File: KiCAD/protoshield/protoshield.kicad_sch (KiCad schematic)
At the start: 35 parts, among them J1 Screw_Terminal_01x03, J2 Screw_Terminal_01x02, J3 Screw_Terminal_01x02, J4 Screw_Terminal_01x02, J5 Screw_Terminal_01x02, J6 Screw_Terminal_01x03, J7 Screw_Terminal_01x04, J8 Screw_Terminal_01x03, U2 Metro_ESP32S3

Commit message: revD: DGFET-DAC bias scheme, kit-style xfmr naming, custom footprints, Output LPF project
Architecture refinements since the previous revD commit (f8d7058):

Analog board (vfo_complete, arduino, dac, power sheets):
  * MCP4922 (U4) ch B exposed as DRIVER_BIAS DAC output -> J31 pin 6
    (replaces the +3.3V pin that was on J31 pin 6 before). Analog's U4
    now controls the ss_pa BS170 driver DC bias point directly from
    firmware -- cleaner than the kit's trimmer+Q201 scheme.
  * MCP4728 (U3) ch A/B exposed as PA_Bias_A_Raw / PA_Bias_B_Raw ->
    J31 pins 7, 8. These feed the ss_pa CD74HC4066 fault-switch (U2),
    which gates them to PA_Bias_A/B on the IRF510 gates. On FAULT_N
    low, switch opens -> IRF510 bias collapses -> conduction cuts.
  * Rename pass: Bias_A/B/_Raw labels -> PA_Bias_A/B/_Raw everywhere
    (analog J3 screw-terminal, umbilical J31, ss_pa U2 inputs). Prefix
    disambiguates from DRIVER_BIAS which drives a different stage.
  * J2 (band-select RJ45 to Output LPF board): added RLY_40 provision.
    Pin layout reorganized -- RLY_40 lives at pin 5, pin 6 kept as a
    spare for a future 6th band.

ss_pa board (pa_stage, fault_shutdown, lpf sheets):
  * Driver + final BS170/IRF510 topology drawn following QRP Labs
    10W Linear kit (RF IN -> T201 input xfmr -> BS170 PP driver
    (Q2, Q6) -> T202 interstage -> IRF510 PP finals (Q3, Q4) ->
    T203 bifilar drain feed -> T204 output xfmr -> RF out).
  * Transformer references renamed to match the kit: T201 (input,
    BN61-2402), T202 (interstage, BN61-2402), T203 (drain feed,
    T50-43), T204 (output, BN43-202).
  * Driver bias filter on DRIVER_BIAS: C19 (0.1uF) + C20 (100pF)
    bulk + HF bypass, into T201 secondary CT (pin 4).
  * +3.3V now locally regulated on ss_pa (MCP1700x-330xxTO, U13)
    from +13.8V, powering U1 (LM393) and U2 (CD74HC4066). J31
    pin 6 freed up for DRIVER_BIAS.
  * Duplicate RJ45 J7 deleted (was a leftover from pre-DAC-bias era).
  * J3 (SMA RF input from analog) foo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
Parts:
- C2, C3: footprint (none) -> Capacitor_THT:C_Disc_D6.0mm_W2.5mm_P5.00mm
- J7: footprint (none) -> TerminalBlock_Phoenix:TerminalBlock_Phoenix_MKDS-1,5-4_1x04_P5.00mm_Horizontal
- J8: footprint (none) -> TerminalBlock_Phoenix:TerminalBlock_Phoenix_MKDS-1,5-3_1x03_P5.00mm_Horizontal
- R1, R2: footprint (none) -> Resistor_THT:R_Axial_DIN0207_L6.3mm_D2.5mm_P10.16mm_Horizontal
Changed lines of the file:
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@@
 			)
 		)
-		(property "Footprint" ""
+		(property "Footprint" "TerminalBlock_Phoenix:TerminalBlock_Phoenix_MKDS-1,5-4_1x04_P5.00mm_Horizontal"
 			(at 232.41 104.14 0)
 			(hide yes)
@@
 			)
 		)
-		(property "Footprint" ""
+		(property "Footprint" "Resistor_THT:R_Axial_DIN0207_L6.3mm_D2.5mm_P10.16mm_Horizontal"
 			(at 198.374 87.884 90)
 			(hide yes)
@@
 			)
 		)
-		(property "Footprint" ""
+		(property "Footprint" "Resistor_THT:R_Axial_DIN0207_L6.3mm_D2.5mm_P10.16mm_Horizontal"
 			(at 198.374 85.344 90)
 			(hide yes)
@@
 			)
 		)
-		(property "Footprint" ""
+		(property "Footprint" "Capacitor_THT:C_Disc_D6.0mm_W2.5mm_P5.00mm"
 			(at 195.2752 96.52 0)
 			(hide yes)
@@
 			)
 		)
-		(property "Footprint" ""
+		(property "Footprint" "Capacitor_THT:C_Disc_D6.0mm_W2.5mm_P5.00mm"
 			(at 193.3448 78.74 0)
 			(hide yes)
@@
 			)
 		)
-		(property "Footprint" ""
+		(property "Footprint" "TerminalBlock_Phoenix:TerminalBlock_Phoenix_MKDS-1,5-3_1x03_P5.00mm_Horizontal"
 			(at 213.36 88.9 0)
 			(hide yes)

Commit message: revD: ss_pa Option C 5V rail + analog SW1 THT + R/C footprints + doc refresh
ss_pa Option C: swap U13 to LM2936Z-5.0 (full +5V logic rail), re-size
R10 10K->6.8K to preserve ~0.3V fault trip at new rail, drop +3.3V net
entirely. Fixes the previously-dead +5V bus that had no source.

Analog SW1 (Si5351 bringup DPDT): swap SMD footprint for
Button_Switch_THT:SW_CK_JS202011CQN_DPDT_Straight. Verified pin-numbering
convention (pin 1 above pin 6 in THT) matches user's intended DPST
wiring; both SDA/SCL break together.

Analog: assign missing footprints to R3/R4/R5/R8/R9 (DIN0207 axial) and
C4/C5/C6/C7/C8 (disc ceramic 5mm). Add xmitter:DIP-14_W7.62mm.kicad_mod
and 74HCT125 symbol to the xmitter library.

Documentation: Rev D handoff doc updated with M1-M8 fix status, Option C
notes, I2C bus voltage architecture, 74HCT125 SPI shifter, FAULT_N
divider details, and Metro-no-footprint note. Supporting docs updated:
i2c_bus.md full rewrite for 5V HV bus + STEMMA reroute, revD_interconnect
board inventory refresh, status banners on ss_pa.md / Master_Description /
cw_envelope_keyer / front_panel_interface pointing to handoff doc for
items beyond their last-current date.

Co-Authored-By: Claude Opus 4.7 <noreply@anthropic.com>
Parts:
- removed J7: Screw_Terminal_01x04, TerminalBlock_Phoenix:TerminalBlock_Phoenix_MKDS-1,5-4_1x04_P5.00mm_Horizontal, symbol Connector:Screw_Terminal_01x04
- added J17: Screw_Terminal_01x05, TerminalBlock_Phoenix:TerminalBlock_Phoenix_MKDS-1,5-5_1x05_P5.00mm_Horizontal, symbol Connector:Screw_Terminal_01x05
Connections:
- net CS_DAC: now also J17.5 (Pin_5)
- net DAC_LDAC_N: now also J17.2 (Pin_2)
- net GND: now also J17.1 (Pin_1)
- net MOSI: now also J17.4 (Pin_4)
- net SCK: now also J17.3 (Pin_3)
- net FAULT_N renamed FAULT_N_CLEAN
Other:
- moved on the sheet: J8
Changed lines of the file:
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@@
 	(wire
 		(pts
-			(xy 208.28 86.36) (xy 201.93 86.36)
+			(xy 217.17 86.36) (xy 201.93 86.36)
 		)
 		(stroke
@@
 	(wire
 		(pts
-			(xy 208.28 88.9) (xy 201.93 88.9)
+			(xy 217.17 88.9) (xy 201.93 88.9)
 		)
 		(stroke
@@
 		)
 	)
-	(global_label "FAULT_N"
+	(global_label "FAULT_N_CLEAN"
 		(shape input)
 		(at 161.29 91.44 0)
@@
 		)
 		(property "Intersheetrefs" "${INTERSHEET_REFS}"
-			(at 172.0767 91.44 0)
+			(at 178.9105 91.44 0)
 			(hide yes)
 			(show_name no)
@@
 	)
 	(global_label "DAC_LDAC_N"
-		(shape output)
-		(at 213.36 109.22 0)
+		(shape input)
+		(at 227.33 109.22 180)
 		(fields_autoplaced yes)
 		(effects
@@
 				(size 1.27 1.27)
 			)
-			(justify left)
+			(justify right)
 		)
 		(property "Intersheetrefs" "${INTERSHEET_REFS}"
-			(at 227.8962 109.22 0)
+			(at 212.7938 109.22 0)
 			(hide yes)
 			(show_name no)
@@
 					(size 1.27 1.27)
 				)
-				(justify left)
+				(justify right)
 			)
 		)
@@
 		)
 	)
-	(global_label "FAULT_N"
+	(global_label "FAULT_N_CLEAN"
 		(shape output)
-		(at 208.28 91.44 180)
+		(at 217.17 91.44 180)
 		(fields_autoplaced yes)
 		(effects
@@
 		)
 		(property "Intersheetrefs" "${INTERSHEET_REFS}"
-			(at 197.4933 91.44 0)
+			(at 199.5495 91.44 0)
 			(hide yes)
 			(show_name no)
@@
 	)
 	(symbol
-		(lib_id "Connector:Screw_Terminal_01x04")
-		(at 232.41 104.14 0)
-		(unit 1)
-		(body_style 1)
-		(exclude_from_sim no)
-		(in_bom yes)
-		(on_board yes)
-		(in_pos_files yes)
-		(dnp no)
-		(fields_autoplaced yes)
-		(property "Reference" "J7"
-			(at 234.95 104.1399 0)
-			(show_name no)
-			(do_not_autoplace no)
-			(effects
-				(font
-					(size 1.27 1.27)
-				)
-				(justify left)
-			)
-		)
-		(property "Value" "Screw_Terminal_01x04"
-			(at 234.95 106.6799 0)
-			(show_name no)
-			(do_not_autoplace no)
-			(effects
-				(font
-					(size 1.27 1.27)
-				)
-				(justify left)
-			)
-		)
-		(property "Footprint" "TerminalBlock_Phoenix:TerminalBlock_Phoenix_MKDS-1,5-4_1x04_P5.00mm_Horizontal"
-			(at 232.41 104.14 0)
-			(hide yes)
-			(show_name no)
-			(do_not_autoplace no)
-			(effects
-				(font
-					(size 1.27 1.27)
-				)
-			)
-		)
-		(property "Datasheet" ""
-			(at 232.41 104.14 0)
-			(hide yes)
-			(show_name no)
-			(do_not_autoplace no)
-			(effects
-				(font
-					(size 1.27 1.27)
-				)
-			)
-		)
-		(property "Description" "Generic screw terminal, single row, 01x04, script generated (kicad-library-utils/schlib/autogen/connector/)"
-			(at 232.41 104.14 0)
-			(hide yes)
-			(show_name no)
-			(do_not_autoplace no)
-			(effects
-				(font
-					(size 1.27 1.27)
-				)
-			)
-		)
-		(pin "3"
-		)
-		(pin "4"
-		)
-		(pin "2"
-		)
-		(pin "1"
-		)
-		(instances
-			(project "protoshield"
-				(path "/90f14230-179e-419d-8d57-3db6b8a7c39f"
-					(reference "J7")
-					(unit 1)
-				)
-			)
-		)
-	)
-	(symbol
 		(lib_id "power:GND")
 		(at 43.18 168.91 0)
@@
 		(in_pos_files yes)
 		(dnp no)
-		(fields_autoplaced yes)
 		(property "Reference" "#PWR014"
 			(at 227.33 78.74 0)
@@
 		)
 		(property "Value" "+3.3V"
-			(at 227.33 87.63 0)
+			(at 231.648 85.09 0)
 			(show_name no)
 			(do_not_autoplace no)
@@
 	(symbol
 		(lib_id "power:GND")
+		(at 227.33 111.76 0)
+		(unit 1)
+		(body_style 1)
+		(exclude_from_sim no)
+		(in_bom yes)
+		(on_board yes)
+		(in_pos_files yes)
+		(dnp no)
+		(fields_autoplaced yes)
+		(property "Reference" "#PWR024"
+			(at 227.33 118.11 0)
+			(hide yes)
+			(show_name no)
+			(do_not_autoplace no)
+			(effects
+				(font
+					(size 1.27 1.27)
+				)
+			)
+		)
+		(property "Value" "GND"
+			(at 227.33 116.84 0)
+			(show_name no)
+			(do_not_autoplace no)
+			(effects
+				(font
+					(size 1.27 1.27)
+				)
+			)
+		)
+		(property "Footprint" ""
+			(at 227.33 111.76 0)
+			(hide yes)
+			(show_name no)
+			(do_not_autoplace no)
+			(effects
+				(font
+					(size 1.27 1.27)
+				)
+			)
+		)
+		(property "Datasheet" ""
+			(at 227.33 111.76 0)
+			(hide yes)
+			(show_name no)
+			(do_not_autoplace no)
+			(effects
+				(font
+					(size 1.27 1.27)
+				)
+			)
+		)
+		(property "Description" "Power symbol creates a global label with name \"GND\" , ground"
+			(at 227.33 111.76 0)
+			(hide yes)
+			(show_name no)
+			(do_not_autoplace no)
+			(effects
+				(font
+					(size 1.27 1.27)
+				)
+			)
+		)
+		(pin "1"
+		)
+		(instances
+			(project "protoshield"
+				(path "/90f14230-179e-419d-8d57-3db6b8a7c39f"
+					(reference "#PWR024")
+					(unit 1)
+				)
+			)
+		)
+	)
+	(symbol
+		(lib_id "power:GND")
 		(at 128.27 69.85 270)
 		(unit 1)
@@
 	)
 	(symbol
+		(lib_id "Connector:Screw_Terminal_01x05")
+		(at 232.41 106.68 0)
+		(mirror x)
+		(unit 1)
+		(body_style 1)
+		(exclude_from_sim no)
+		(in_bom yes)
+		(on_board yes)
+		(in_pos_files yes)
+		(dnp no)
+		(property "Reference" "J17"
+			(at 232.41 95.25 0)
+			(show_name no)
+			(do_not_autoplace no)
+			(effects
+				(font
+					(size 1.27 1.27)
+				)
+			)
+		)
+		(property "Value" "Screw_Terminal_01x05"
+			(at 232.41 97.79 0)
+			(show_name no)
+			(do_not_autoplace no)
+			(effects
+				(font
+					(size 1.27 1.27)
+				)
+			)
+		)
+		(property "Footprint" "TerminalBlock_Phoenix:TerminalBlock_Phoenix_MKDS-1,5-5_1x05_P5.00mm_Horizontal"
+			(at 232.41 106.68 0)
+			(hide yes)
+			(show_name no)
+			(do_not_autoplace no)
+			(effects
+				(font
+					(size 1.27 1.27)
+				)
+			)
+		)
+		(property "Datasheet" ""
+			(at 232.41 106.68 0)
+			(hide yes)
+			(show_name no)
+			(do_not_autoplace no)
+			(effects
+				(font
+					(size 1.27 1.27)
+				)
+			)
+		)
+		(property "Description" "Generic screw terminal, single row, 01x05, script generated (kicad-library-utils/schlib/autogen/connector/)"
+			(at 232.41 106.68 0)
+			(hide yes)
+			(show_name no)
+			(do_not_autoplace no)
+			(effects
+				(font
+					(size 1.27 1.27)
+				)
+			)
+		)
+		(pin "1"
+		)
+		(pin "4"
+		)
+		(pin "5"
+		)
+		(pin "2"
+		)
+		(pin "3"
+		)
+		(instances
+			(project "protoshield"
+				(path "/90f14230-179e-419d-8d57-3db6b8a7c39f"
+					(reference "J17")
+					(unit 1)
+				)
+			)
+		)
+	)
+	(symbol
 		(lib_id "xmitter:1N4728A")
 		(at 44.45 59.69 270)
@@
 	(symbol
 		(lib_id "Connector:Screw_Terminal_01x03")
-		(at 213.36 88.9 0)
+		(at 222.25 88.9 0)
 		(unit 1)
 		(body_style 1)
@@
 		(fields_autoplaced yes)
 		(property "Reference" "J8"
-			(at 215.9 87.6299 0)
+			(at 224.79 87.6299 0)
 			(show_name no)
 			(do_not_autoplace no)
@@
 		)
 		(property "Value" "Screw_Terminal_01x03"
-			(at 215.9 90.1699 0)
+			(at 224.79 90.1699 0)
 			(show_name no)
 			(do_not_autoplace no)
@@
 		)
 		(property "Footprint" "TerminalBlock_Phoenix:TerminalBlock_Phoenix_MKDS-1,5-3_1x03_P5.00mm_Horizontal"
-			(at 213.36 88.9 0)
+			(at 222.25 88.9 0)
 			(hide yes)
 			(show_name no)
@@
 		)
 		(property "Datasheet" ""
-			(at 213.36 88.9 0)
+			(at 222.25 88.9 0)
 			(hide yes)
 			(show_name no)
@@
 		)
 		(property "Description" "Generic screw terminal, single row, 01x03, script generated (kicad-library-utils/schlib/autogen/connector/)"
-			(at 213.36 88.9 0)
+			(at 222.25 88.9 0)
 			(hide yes)
 			(show_name no)

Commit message: revD analog: L1 Bourns 78F footprint + CD74HC4050E xmitter lib additions
Analog L1 (270nH Bourns 78F RF choke) gets footprint
Inductor_THT:L_Axial_L7.0mm_D3.3mm_P10.16mm_Horizontal_Fastron_MICC
(stock KiCad; 78F body 7.11x2.79mm fits within the MICC silk envelope).

Added to xmitter library:
- symbol CD74HC4050E (hex non-inverting buffer, DIP-16, standard 4050
  pinout, pre-linked to xmitter:DIP-16_W7.62mm footprint)
- footprint xmitter:DIP-16_W7.62mm (verbatim copy of stock
  Package_DIP:DIP-16_W7.62mm so the lib is self-contained)

Other sheet / project / netlist touches picked up from the recent
session work on analog test sheet and protoshield.

Co-Authored-By: Claude Opus 4.7 <noreply@anthropic.com>
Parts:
- removed D3, D4: 1N4728A, Diode_THT:D_DO-41_SOD81_P10.16mm_Horizontal, symbol xmitter:1N4728A
- removed J17: Screw_Terminal_01x05, TerminalBlock_Phoenix:TerminalBlock_Phoenix_MKDS-1,5-5_1x05_P5.00mm_Horizontal, symbol Connector:Screw_Terminal_01x05
- added J16: Screw_Terminal_01x05, TerminalBlock_Phoenix:TerminalBlock_Phoenix_MKDS-1,5-5_1x05_P5.00mm_Horizontal, symbol Connector:Screw_Terminal_01x05
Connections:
- net CS_DAC: now also J16.4 (Pin_4)
- net DAC_LDAC_N: now also J16.5 (Pin_5)
- net GND: now also J16.1 (Pin_1)
- net MOSI: now also J16.3 (Pin_3)
- net SCK: now also J16.2 (Pin_2)

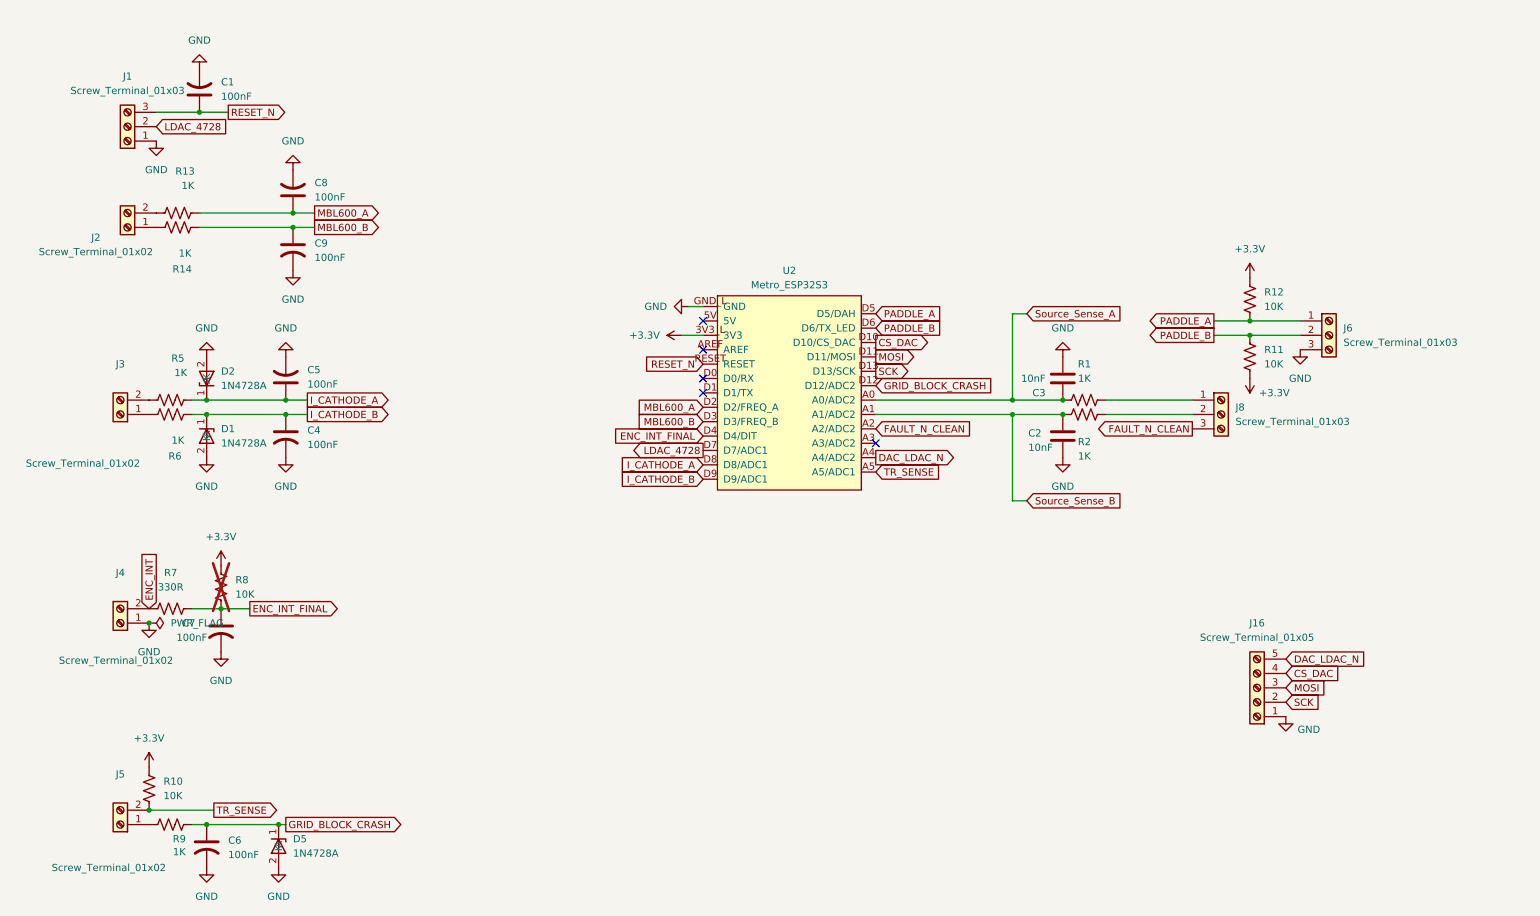
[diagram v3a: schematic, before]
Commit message: revD: frontpanel + Output LPF text updates + protoshield in-progress
Output LPF: K relay Description text fix (pole 2 NC/COM/NO -> NO/COM/NC)
on K1/K2/K3 instances and the embedded lib symbol; CF7/CF8/CF12/CF16
Description "Unpolarized capacitor 2 in parallel to reach" stripped
back to "Unpolarized capacitor"; L6-L20 Descriptions updated T68-6 ->
T50-6 to match footprints.

xmitter.kicad_sym Relay_G6K Description text fix (pole 2 NC/COM/NO ->
NO/COM/NC) so future placements come out right.

Frontpanel: user updates (netlist regenerated).

Protoshield: in-progress schematic touches (new J7, #PWR017). Netlist
intentionally stale -- will regen after Metro-symbol SDA/SCL addition.

Co-Authored-By: Claude Opus 4.7 <noreply@anthropic.com>
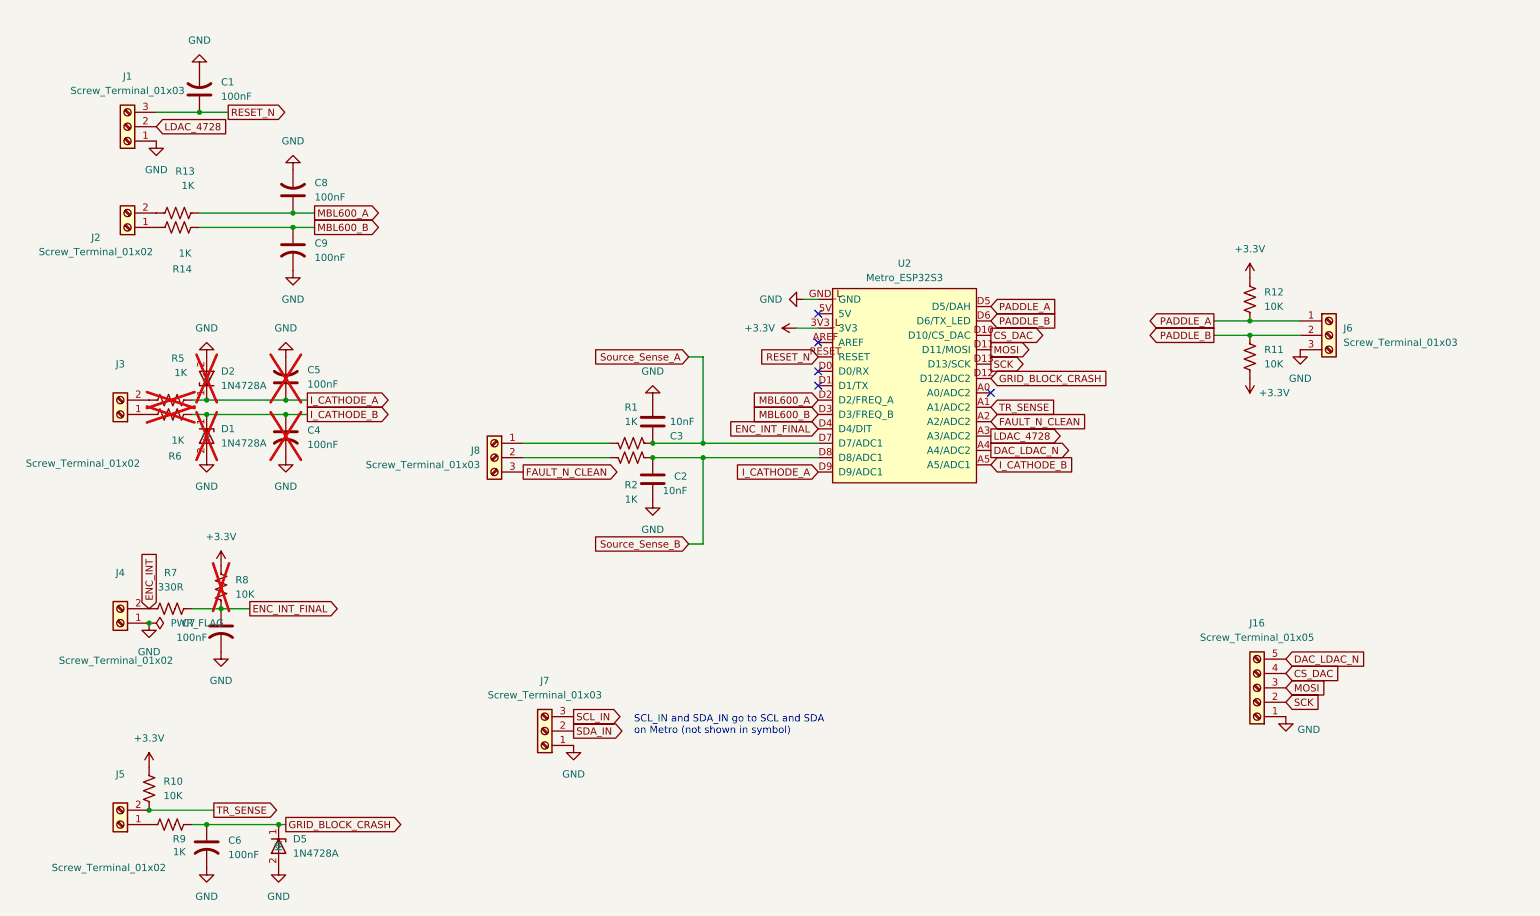
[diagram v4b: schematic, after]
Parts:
- added J7: Screw_Terminal_01x03, TerminalBlock_Phoenix:TerminalBlock_Phoenix_MKDS-1,5-3_1x03_P5.00mm_Horizontal, symbol Connector:Screw_Terminal_01x03
- C4, C5, D1, D2, R5, R6: now not fitted
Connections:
- net GND: now also J7.1 (Pin_1)
- net I_CATHODE_A: now also U2.D9 (D9/ADC1); no longer U2.D8 (D8/ADC1)
- net I_CATHODE_B: now also U2.A5 (A5/ADC1); no longer U2.D9 (D9/ADC1)
- net LDAC_4728: now also U2.A3 (A3/ADC2); no longer U2.D7 (D7/ADC1)
- net Source_Sense_A: now also U2.D7 (D7/ADC1); no longer U2.A0 (A0/ADC2)
- net Source_Sense_B: now also U2.D8 (D8/ADC1); no longer U2.A1 (A1/ADC2)
- net TR_SENSE: now also U2.A1 (A1/ADC2); no longer U2.A5 (A5/ADC1)
- new net SCL_IN: J7.3 (Pin_3)
- new net SDA_IN: J7.2 (Pin_2)
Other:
- note added: "SCL_IN and SDA_IN go to SCL and SDA on Metro (not shown in symbol)"
- moved on the sheet: U2
